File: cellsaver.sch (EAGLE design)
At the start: 31 parts, among them Q11 2PMOS30V_4.5A, Q21 2PMOS30V_4.5A, Q22 2PMOS30V_4.5A, Q31 2PMOS30V_4.5A, Q32 2PMOS30V_4.5A, Q41 2PMOS30V_4.5A, Q42 2PMOS30V_4.5A, Q51 2PMOS30V_4.5A, Q52 2PMOS30V_4.5A, Q61 2PMOS30V_4.5A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

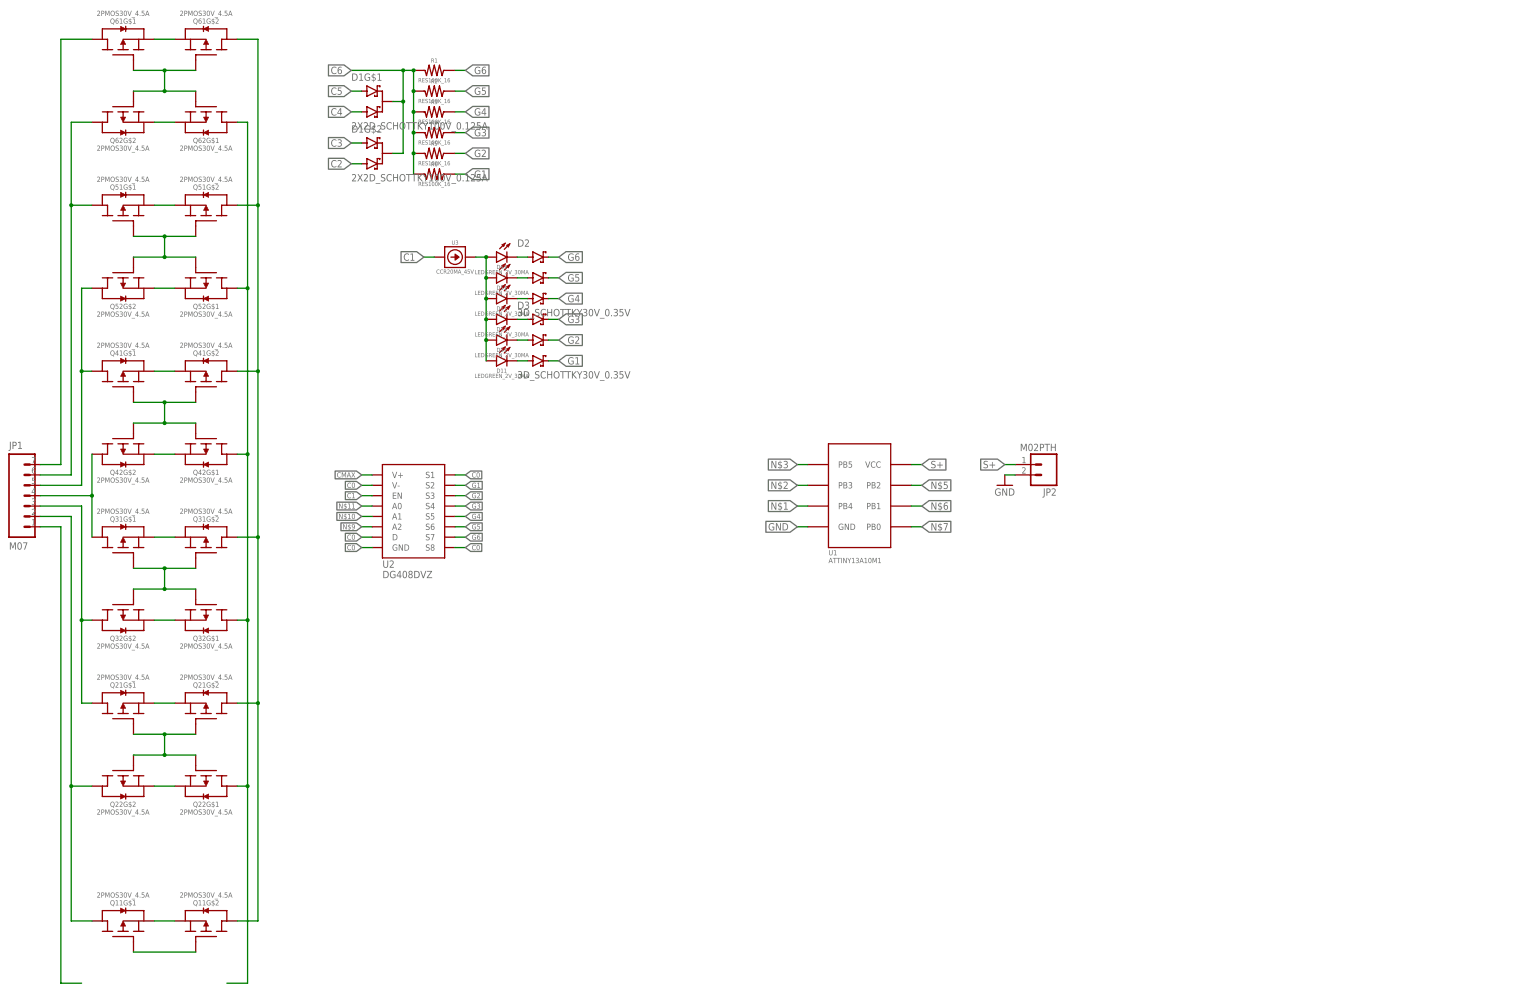
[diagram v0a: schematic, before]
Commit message: FET change, layout
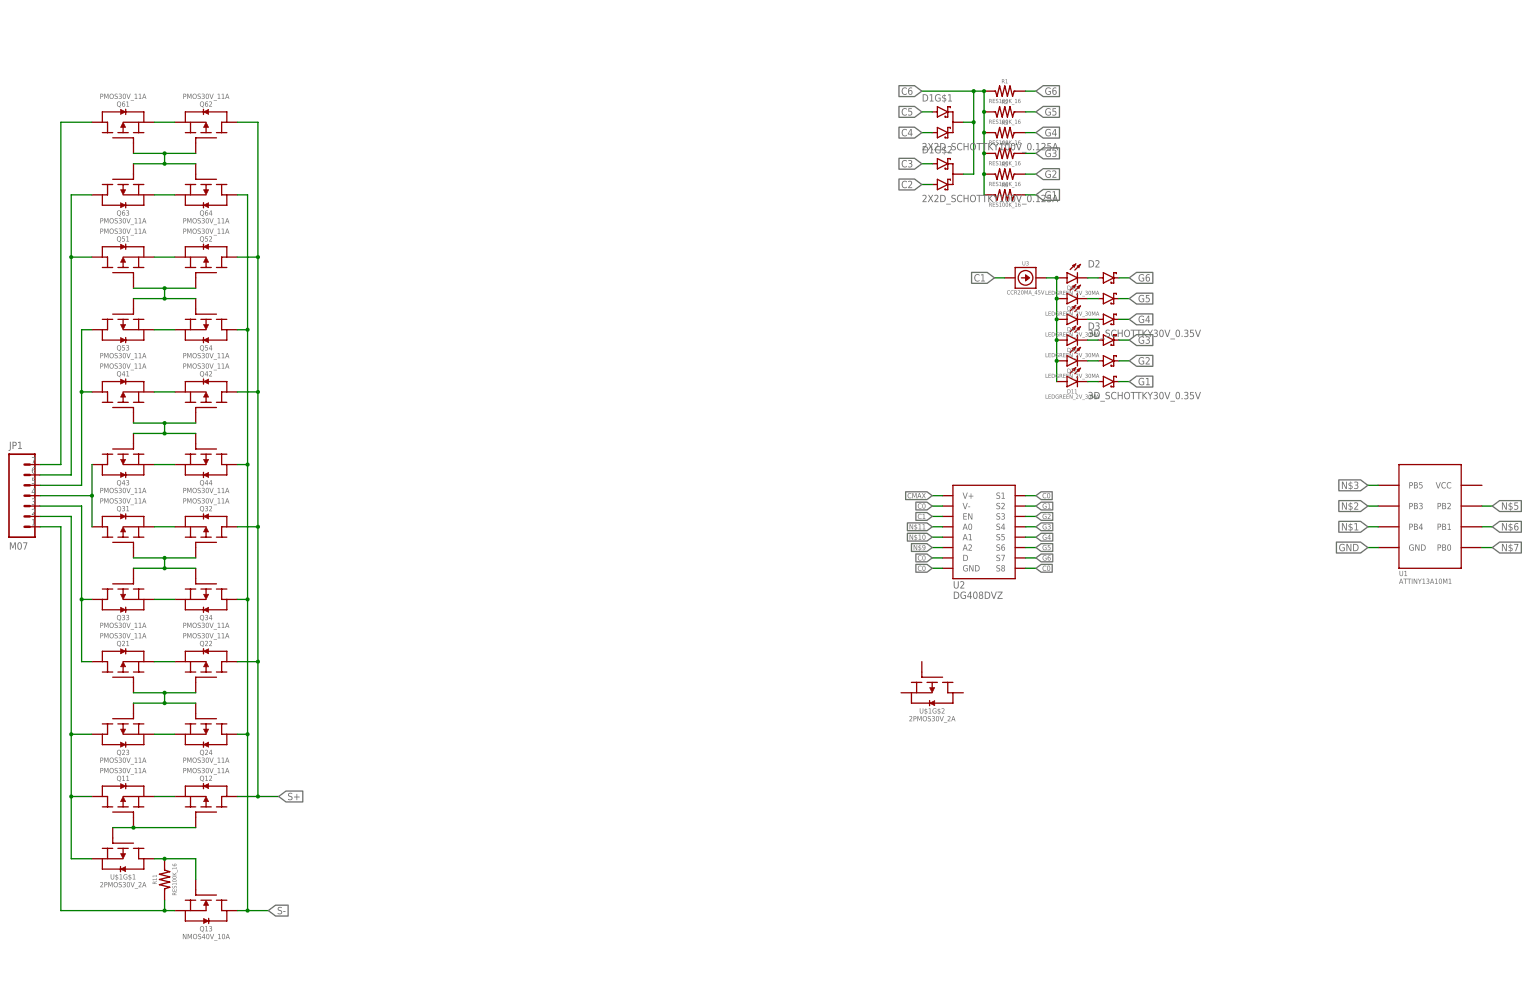
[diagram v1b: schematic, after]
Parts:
- removed JP2: M02PTH, SparkFun-Connectors:M02PTH
- added Q12, Q23, Q24, Q33, Q34, Q43, Q44, Q53, Q54, Q63, Q64: PMOS30V_11A, dubec:PMOS30V_11A
- added Q13: NMOS40V_10A, dubec:NMOS40V_10A
- added R11: RES100K_16, dubec:RES100K_16
- added U$1: 2PMOS30V_2A, dubec:2PMOS30V_2A
- Q11, Q21, Q22, Q31, Q32, Q41, Q42, Q51, Q52, Q61, Q62: value 2PMOS30V_4.5A -> PMOS30V_11A; device dubec:2PMOS30V_4.5A -> dubec:PMOS30V_11A
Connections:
- removed net S+1: Q11G$1.S, Q11G$2.S
- removed net S+2: Q21G$1.S, Q21G$2.S
- removed net S+3: Q31G$1.S, Q31G$2.S
- removed net S+4: Q41G$1.S, Q41G$2.S
- removed net S+5: Q51G$1.S, Q51G$2.S
- removed net S+6: Q61G$1.S, Q61G$2.S
- removed net S-2: Q22G$1.S, Q22G$2.S
- removed net S-3: Q32G$1.S, Q32G$2.S
- removed net S-4: Q42G$1.S, Q42G$2.S
- removed net S-5: Q52G$1.S, Q52G$2.S
- removed net S-6: Q62G$1.S, Q62G$2.S
- removed net T+: Q11G$2.D, Q21G$2.D, Q31G$2.D, Q41G$2.D, Q51G$2.D, Q61G$2.D
- removed net T-: Q22G$1.D, Q32G$1.D, Q42G$1.D, Q52G$1.D, Q62G$1.D
- new net G01: Q13.G, R11.2, U$1G$1.D
- new net G11: Q11.G, Q12.G, U$1G$1.G
- new net G21: Q21.G, Q22.G, Q23.G, Q24.G
- new net G31: Q31.G, Q32.G, Q33.G, Q34.G
- new net G41: Q41.G, Q42.G, Q43.G, Q44.G
- new net G51: Q51.G, Q52.G, Q53.G, Q54.G
- new net G61: Q61.G, Q62.G, Q63.G, Q64.G
- new net S+11: Q11.S, Q12.S
- new net S+21: Q21.S, Q22.S
- new net S+31: Q31.S, Q32.S
- new net S+41: Q41.S, Q42.S
- new net S+51: Q51.S, Q52.S
- new net S+61: Q61.S, Q62.S
- new net S-: Q13.D, Q24.D, Q34.D, Q44.D, Q54.D, Q64.D
- new net S-21: Q23.S, Q24.S
- new net S-31: Q33.S, Q34.S
- new net S-41: Q43.S, Q44.S
- new net S-51: Q53.S, Q54.S
- new net S-61: Q63.S, Q64.S
- net C0: now also Q13.S, R11.1
- net C1: now also Q11.D, Q23.D, U$1G$1.S; no longer Q11G$1.D, Q22G$2.D
- net C2: now also Q21.D, Q33.D; no longer Q21G$1.D, Q32G$2.D
- net C3: now also Q31.D, Q43.D; no longer Q31G$1.D, Q42G$2.D
- net C4: now also Q41.D, Q53.D; no longer Q41G$1.D, Q52G$2.D
- net C5: now also Q51.D, Q63.D; no longer Q51G$1.D, Q62G$2.D
- net C6: now also Q61.D; no longer Q61G$1.D
- net G1: no longer Q11G$1.G, Q11G$2.G
- net G2: no longer Q21G$1.G, Q21G$2.G, Q22G$1.G, Q22G$2.G
- net G3: no longer Q31G$1.G, Q31G$2.G, Q32G$1.G, Q32G$2.G
- net G4: no longer Q41G$1.G, Q41G$2.G, Q42G$1.G, Q42G$2.G
- net G5: no longer Q51G$1.G, Q51G$2.G, Q52G$1.G, Q52G$2.G
- net G6: no longer Q61G$1.G, Q61G$2.G, Q62G$1.G, Q62G$2.G
- net GND: no longer JP2.2
- net N$12: now also D2.A2
- net N$14: now also D3.A1
- net N$15: now also D3.A2
- net N$16: now also D3.A3
- net S+: now also Q12.D, Q22.D, Q32.D, Q42.D, Q52.D, Q62.D; no longer JP2.1, U1.VCC
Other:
- moved on the sheet: D11, D1G$1, D1G$2, D2, D21, D3, D31, D41, D51, D61, Q11, Q21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

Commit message: Second pair of rails, for direct contact
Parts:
- removed Q61, Q63: PMOS30V_11A, dubec:PMOS30V_11A
- added Q15, Q16, Q25, Q26, Q27, Q28, Q35, Q36, Q37, Q38, Q45, Q46, Q47, Q48, Q55, Q56, Q57, Q58, Q66, Q68: PMOS30V_11A, dubec:PMOS30V_11A
- added Q17: NMOS40V_10A, dubec:NMOS40V_10A
- added R7: RES100K_16, dubec:RES100K_16
- JP1: value M07 -> M07XHRA; device dubec:M07 -> dubec:M07XHRA
- renumbered U$1 to Q14
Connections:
- removed net G1: D3.C3, R6.2, U2.S2
- removed net G2: D3.C2, R5.2, U2.S3
- removed net G3: D3.C1, R4.2, U2.S4
- removed net G4: D2.C3, R3.2, U2.S5
- removed net G5: D2.C2, R2.2, U2.S6
- removed net G6: D2.C1, R1.2, U2.S7
- removed net S+61: Q61.S, Q62.S
- removed net S-61: Q63.S, Q64.S
- new net G02: Q14G$2.D, Q17.G, R7.2
- new net G12: Q14G$2.G, Q15.G, Q16.G
- new net G22: Q25.G, Q26.G, Q27.G, Q28.G
- new net G32: Q35.G, Q36.G, Q37.G, Q38.G
- new net G42: Q45.G, Q46.G, Q47.G, Q48.G
- new net G52: Q55.G, Q56.G, Q57.G, Q58.G
- new net G62: Q66.G, Q68.G
- new net S+12: Q15.S, Q16.S
- new net S+22: Q25.S, Q26.S
- new net S+32: Q35.S, Q36.S
- new net S+42: Q45.S, Q46.S
- new net S+52: Q55.S, Q56.S
- new net S-22: Q27.S, Q28.S
- new net S-32: Q37.S, Q38.S
- new net S-42: Q47.S, Q48.S
- new net S-52: Q57.S, Q58.S
- new net T+: Q16.D, Q26.D, Q36.D, Q46.D, Q56.D, Q66.D
- new net T-: Q17.D, Q28.D, Q38.D, Q48.D, Q58.D, Q68.D
- net C0: now also JP1.7, Q17.S, R7.1; no longer JP1.1
- net C1: now also JP1.6, Q14G$2.S, Q15.D, Q27.D; no longer JP1.2
- net C2: now also JP1.5, Q25.D, Q37.D; no longer JP1.3
- net C3: now also Q35.D, Q47.D
- net C4: now also JP1.3, Q45.D, Q57.D; no longer JP1.5
- net C5: now also JP1.2, Q55.D, Q64.S, Q68.S; no longer JP1.6, Q63.D
- net C6: now also JP1.1, Q62.S, Q66.S; no longer JP1.7, Q61.D
- net G11: now also D3.C3, R6.2, U2.S2
- net G21: now also D3.C2, R5.2, U2.S3
- net G31: now also D3.C1, R4.2, U2.S4
- net G41: now also D2.C3, R3.2, U2.S5
- net G51: now also D2.C2, R2.2, U2.S6
- net G61: now also D2.C1, R1.2, U2.S7; no longer Q61.G, Q63.G
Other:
- moved on the sheet: JP1

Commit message: Bootstrap power, FET optimization
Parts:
- removed Q14: 2PMOS30V_2A, dubec:2PMOS30V_2A
- removed Q24: PMOS30V_11A, dubec:PMOS30V_11A
- removed R6: RES100K_16, dubec:RES100K_16
- added D4, DG1: 4DSCH30V_0A1, dubec:4DSCH30V_0A1
- added Q01: NMOS40V_10A, dubec:NMOS40V_10A
- added R12, RG51, RG61: RES100K_16, dubec:RES100K_16
- added U$1: TCAP330UF_6.3V, dubec:TCAP330UF_6.3V
- D1: value 2X2D_SCHOTTKY100V_0.125A -> 4DSCH30V_0A1; device dubec:2X2D_SCHOTTKY100V_0.125A -> dubec:4DSCH30V_0A1
- Q13: value NMOS40V_10A -> 2PMOS30V_2A; device dubec:NMOS40V_10A -> dubec:2PMOS30V_2A
- R1, R2: value RES100K_16 -> RES4.22K_16; device dubec:RES100K_16 -> dubec:RES4.22K_16
- renumbered Q17 to Q03, R3 to RG41, R4 to RG31, R5 to RG21
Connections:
- removed net C0: JP1.7, Q03.S, Q13.S, R11.1, R7.1, U2.D, U2.GND, U2.S1, U2.S8, U2.V-
- removed net CMAX: U2.V+
- removed net G01: Q13.G, Q14G$1.D, R11.2
- removed net G12: Q14G$2.G, Q15.G, Q16.G
- removed net GND: U1.GND
- removed net S+11: Q11.S, Q12.S
- new net BATT+: D1G$1.C, D1G$2.C, D1G$3.C, D1G$4.C, D4G$3.C, RG21.1, RG31.1, RG41.1, RG51.1, RG61.1, U2.V+
- new net BATT-: JP1.7, Q01.S, Q03.S, R12.1, R7.1, U2.S1
- new net G13: Q13G$2.G, Q15.G, Q16.G
- new net N$17: Q12.G, Q13G$1.D, R12.2
- new net N$18: DG1G$1.A, DG1G$2.A, Q11.G
- new net VCC: D4G$1.C, D4G$2.C, U$1.A, U1.VCC, U2.EN
- net C1: now also Q13G$1.S, Q13G$2.S; no longer Q14G$1.S, Q14G$2.S, Q23.D, U2.EN
- net C2: now also D1G$1.A, R11.1; no longer D1G$2.A2
- net C3: now also D1G$2.A; no longer D1G$2.A1
- net C4: now also D1G$3.A; no longer D1G$1.A2
- net C5: now also D1G$4.A; no longer D1G$1.A1
- net C6: now also D4G$3.A; no longer D1G$1.C, D1G$2.C, R1.1, R2.1, R6.1, RG21.1, RG31.1, RG41.1
- net G02: now also Q13G$2.D; no longer Q14G$2.D
- net G11: now also DG1G$1.C, Q01.G, Q13G$1.G, R11.2; no longer Q11.G, Q12.G, Q14G$1.G, R6.2
- net G21: now also DG1G$2.C; no longer Q24.G
- net G51: now also RG51.2; no longer R2.2
- net G61: now also RG61.2; no longer R1.2
- net S+: now also D4G$1.A, D4G$2.A, R1.2
- net S-: now also Q01.D, Q23.D, R1.1, U$1.C, U1.GND; no longer Q13.D, Q24.D
- net S-21: now also Q11.S, Q12.S; no longer Q24.S
- net T+: now also R2.2
- net T-: now also R2.1
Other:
- moved on the sheet: Q11, Q12, Q13G$1, Q23, R1, R11, R2

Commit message: .
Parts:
- added U$2: TFORM_4_4311_4A4, dubec:TFORM_4_4311_4A4
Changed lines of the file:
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@@
 <part name="R1" library="dubec" deviceset="RES" device="4.22K_16"/>
 <part name="R2" library="dubec" deviceset="RES" device="4.22K_16"/>
+<part name="U$2" library="dubec" deviceset="TFORM_4_4" device="311_4A4"/>
 </parts>
 <sheets>
@@
 <instance part="R1" gate="G$1" x="71.12" y="58.42" rot="R90"/>
 <instance part="R2" gate="G$1" x="142.24" y="55.88" rot="R90"/>
+<instance part="U$2" gate="G$1" x="307.34" y="127"/>
 </instances>
 <busses>
